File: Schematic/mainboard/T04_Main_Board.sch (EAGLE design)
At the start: 14 parts, among them IC1 7805DT, J1 AVR_SPI_PRG_6PTH, U1 ATMEGA328P_PDIP

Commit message: Mainboard Update and Prototype_rev4 update
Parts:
- removed C3, C4, C5: 0.1u, rcl:C-EUC3225
- removed X1, X2, X3: (no value), con-molex:KK-156-4
- added SV3: (no value), con-lsta:FE08-1
- added TP1, TP10, TP11, TP12, TP2, TP3, TP4, TP5, TP6, TP7, TP8, TP9: TPB1,27, testpad:TPB1,27
- C6: device rcl:C-EUC3225 -> rcl:C-EU025-024X044
- R1: value 4.7k -> 10k; device rcl:R-US_0414/5V -> rcl:R-US_M2309
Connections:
- removed net MISO/TRIG3: J1.1, U1.PB4(MISO), X3-1.S
- removed net MOSI/ECHO2: J1.4, U1.PB3(MOSI/OC2), X2-2.S
- removed net SCK/ECHO3: J1.3, U1.PB5(SCK), X3-2.S
- new net ECHO2: SV3.4, TP9.TP, U1.PD7(AIN1)
- new net ECHO3: SV3.6, TP11.TP, U1.PB1(OC1A)
- new net MISO: J1.1, U1.PB4(MISO)
- new net MOSI: J1.4, U1.PB3(MOSI/OC2)
- new net SCK: J1.3, U1.PB5(SCK)
- new net TRIG3: SV3.5, TP10.TP, U1.PB0(ICP)
- net +12V: now also TP12.TP
- net +5V: now also SV3.7, TP1.TP, U1.VCC; no longer C3.1, C4.1, C5.1, X1-3.S, X2-3.S, X3-3.S
- net BIT0: now also TP2.TP, U1.PD0(RXD); no longer U1.PD5(T1)
- net BIT1: now also TP3.TP, U1.PD1(TXD); no longer U1.PD6(AIN0)
- net BIT2: now also TP4.TP, U1.PD2(INT0); no longer U1.PD7(AIN1)
- net BIT3: now also TP5.TP, U1.PD3(INT1); no longer U1.PB0(ICP)
- net ECHO1: now also SV3.2, TP7.TP, U1.PD5(T1); no longer U1.PB1(OC1A), X1-2.S
- net GND: now also SV3.8, U1.GND@1, U1.GND@2; no longer C3.2, C4.2, C5.2, X1-4.S, X2-4.S, X3-4.S
- net TRIG1: now also SV3.1, TP6.TP, U1.PD4(XCK/T0); no longer U1.PD2(INT0), X1-1.S
- net TRIG2: now also SV3.3, TP8.TP, U1.PD6(AIN0); no longer U1.PB2(SS/OC1B), X2-1.S
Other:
- note added: "Connector To display.sch"
- note added: "Connector to programmer"
- note added: "Connnector to sensors"
- note added: "Rusty Wiseman Dan Frister Branden Driver Noah Erickson"
- note removed: "HEADER TO DISPLAY"
- note removed: "SENSOR 1"
- note removed: "SENSOR 2"
- note removed: "SENSOR 3"
- moved on the sheet: C1, C2, C6, IC1, J1, R1, SV1, U1

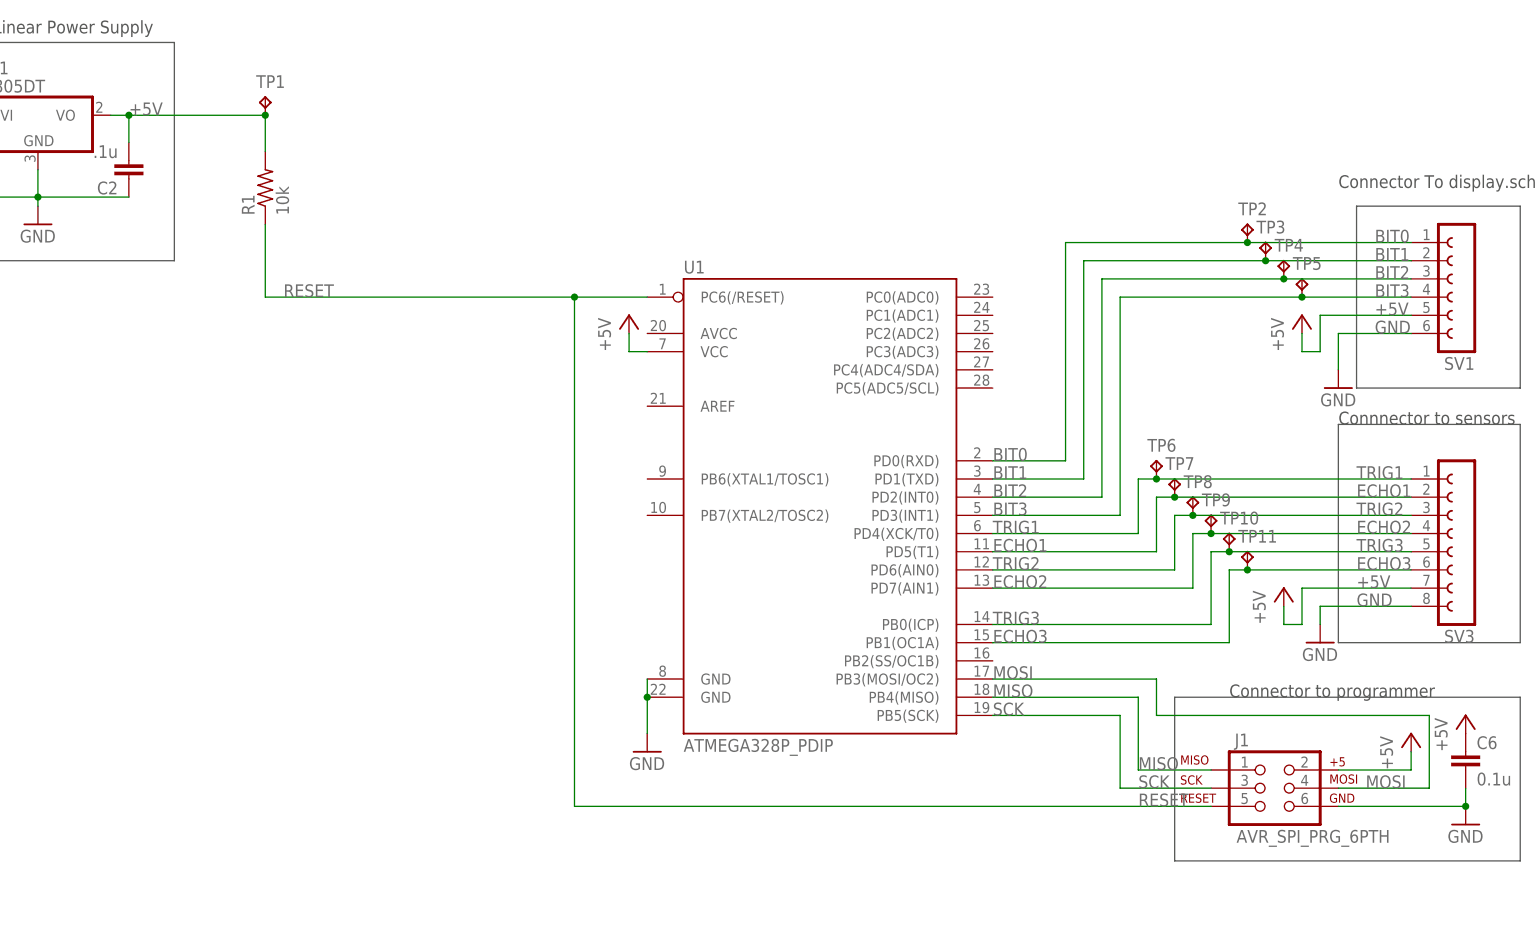
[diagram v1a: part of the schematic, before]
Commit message: Mainboard update - Clock and bypass caps
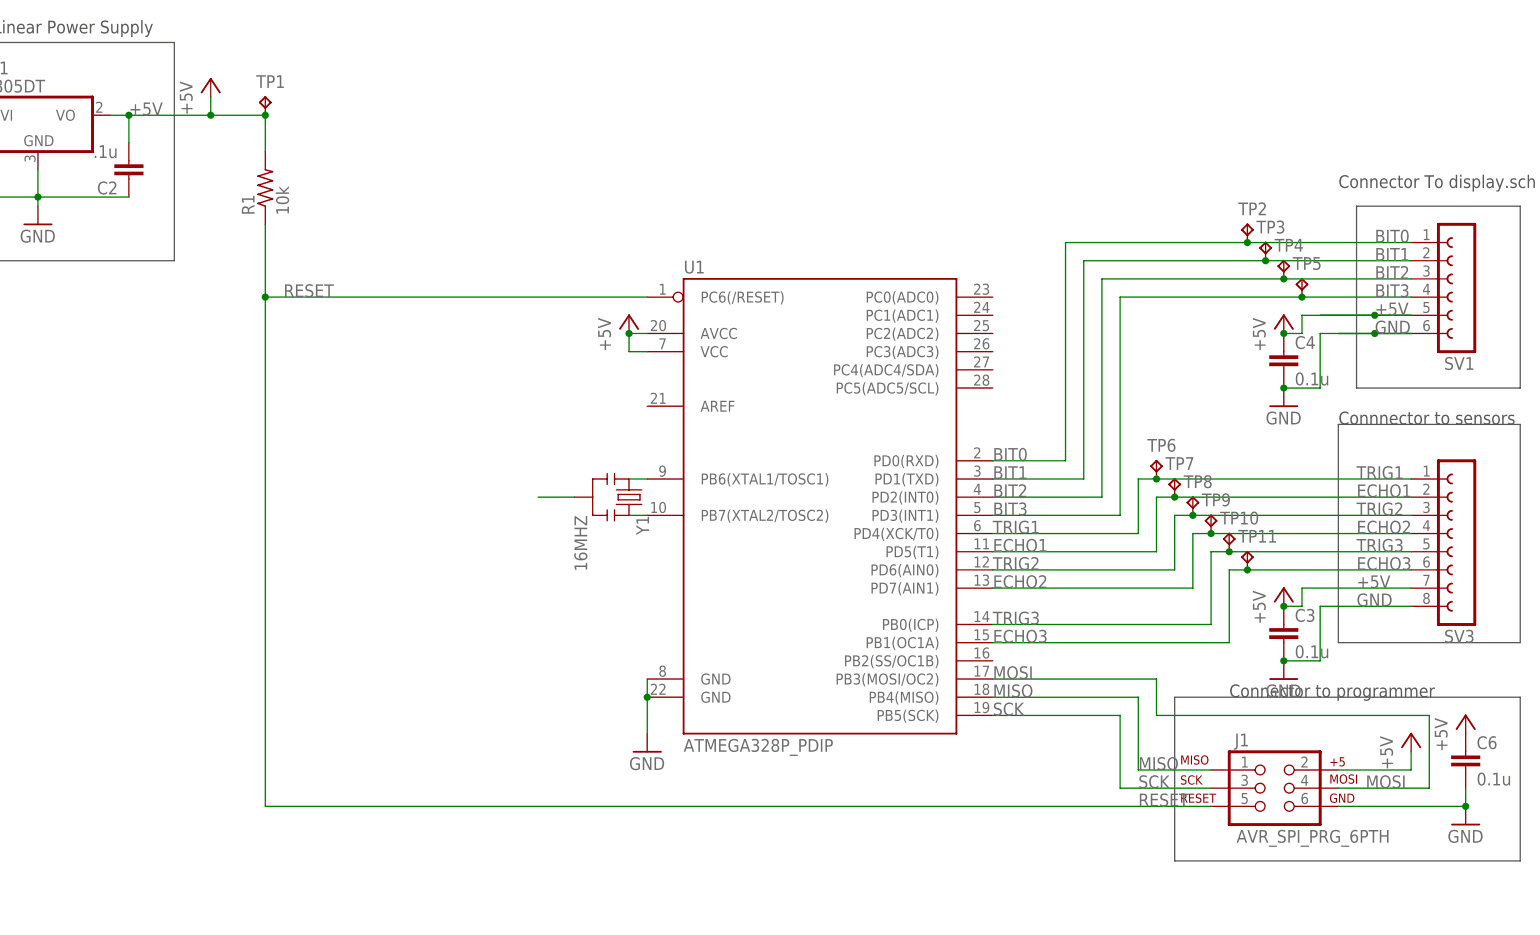
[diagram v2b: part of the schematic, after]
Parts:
- added C3, C4: 0.1u, rcl:C-EU025-024X044
- added Y1: 16MHZ, SparkFun-FreqCtrl:RESONATOR16MHZ
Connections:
- new net N$1: U1.PB6(XTAL1/TOSC1), Y1.1
- new net N$2: U1.PB7(XTAL2/TOSC2), Y1.3
- new net N$3: Y1.2
- net +5V: now also C3.1, C4.1, U1.AVCC
- net GND: now also C3.2, C4.2

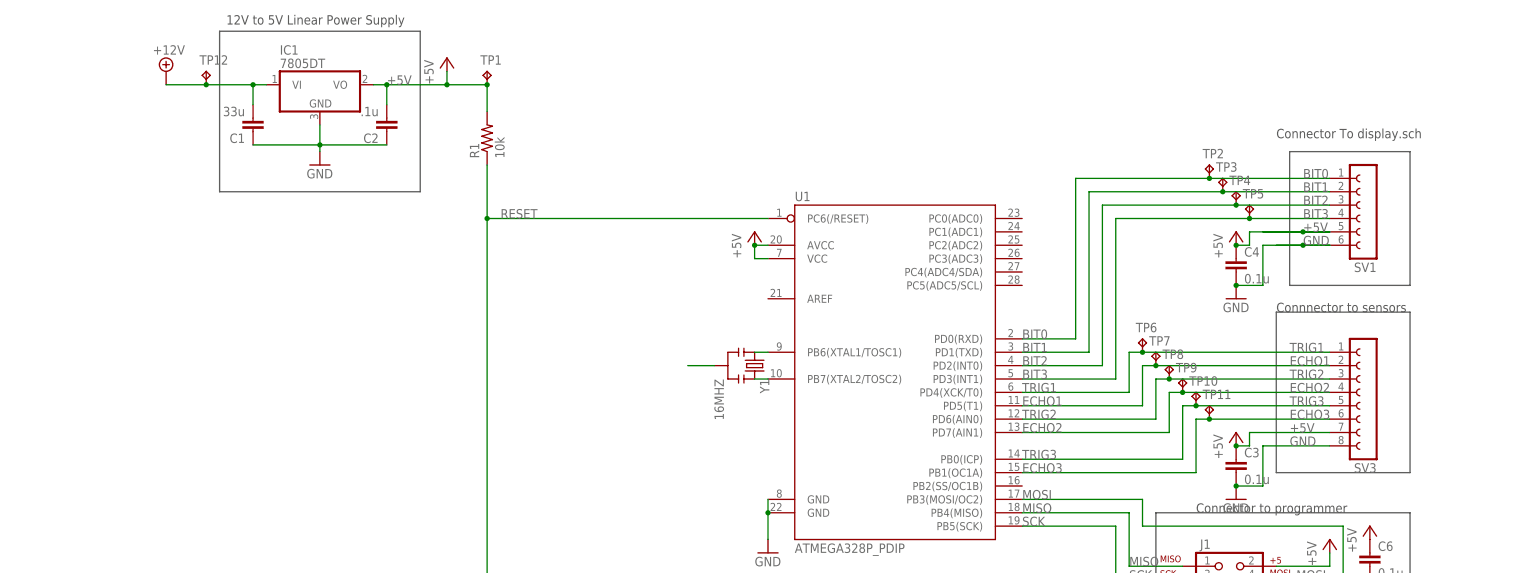
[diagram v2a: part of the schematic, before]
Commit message: Mainboard layout fixed
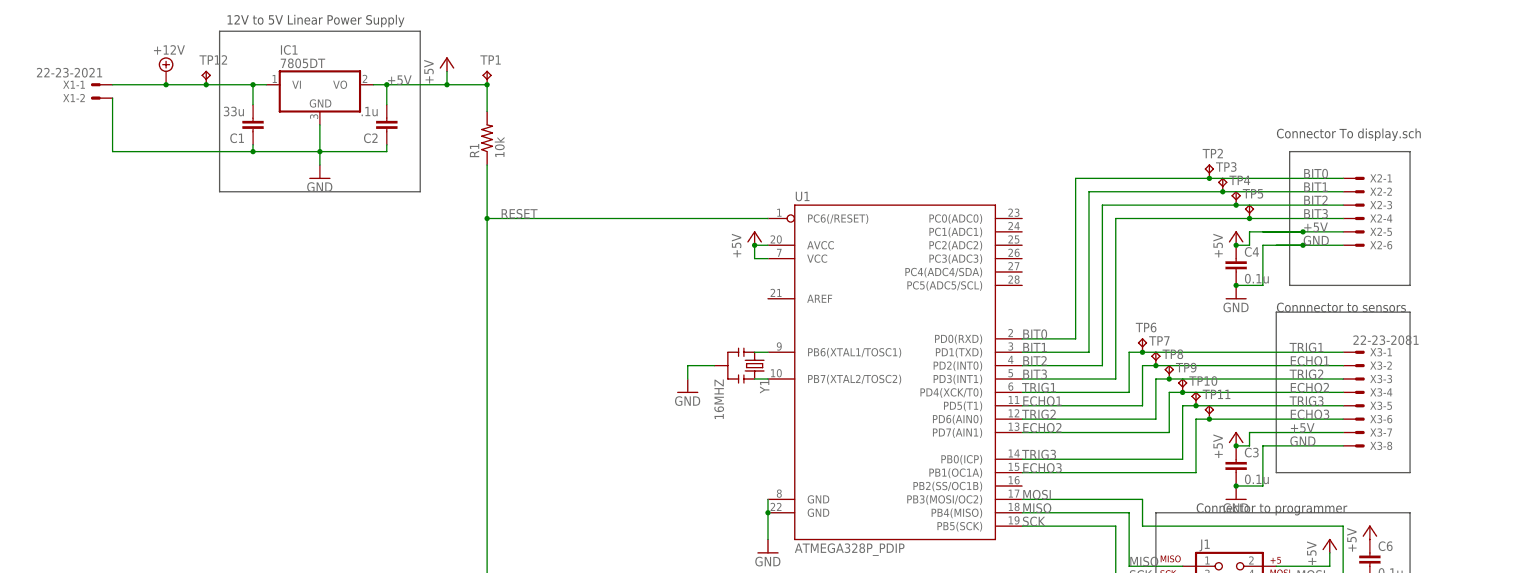
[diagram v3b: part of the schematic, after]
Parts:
- removed SV1: (no value), con-lsta:FE06-1
- removed SV3: (no value), con-lsta:FE08-1
- added X1: 22-23-2021, con-molex:22-23-2021
- added X2: (no value), con-molex:22-23-2061
- added X3: 22-23-2081, con-molex:22-23-2081
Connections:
- removed net N$3: Y1.2
- net +12V: now also X1-1.S
- net +5V: now also X2-5.S, X3-7.S; no longer SV1.5, SV3.7
- net BIT0: now also X2-1.S; no longer SV1.1
- net BIT1: now also X2-2.S; no longer SV1.2
- net BIT2: now also X2-3.S; no longer SV1.3
- net BIT3: now also X2-4.S; no longer SV1.4
- net ECHO1: now also X3-2.S; no longer SV3.2
- net ECHO2: now also X3-4.S; no longer SV3.4
- net ECHO3: now also X3-6.S; no longer SV3.6
- net GND: now also X1-2.S, X2-6.S, X3-8.S, Y1.2; no longer SV1.6, SV3.8
- net TRIG1: now also X3-1.S; no longer SV3.1
- net TRIG2: now also X3-3.S; no longer SV3.3
- net TRIG3: now also X3-5.S; no longer SV3.5

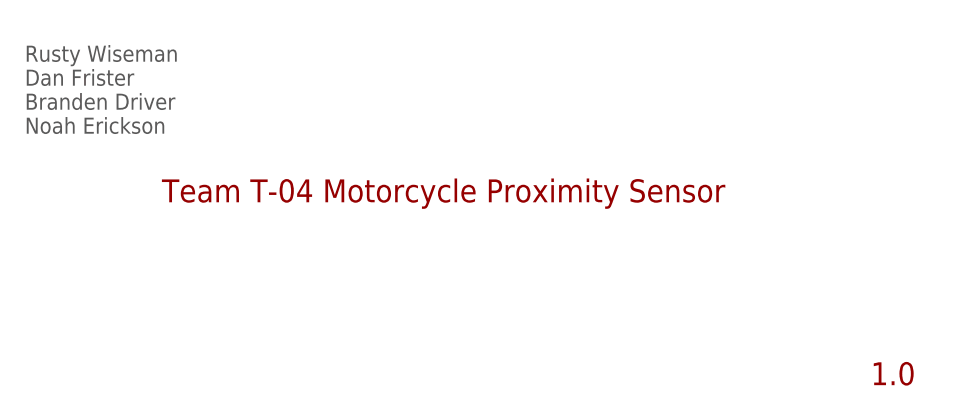
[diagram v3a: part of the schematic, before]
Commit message: Reverified ERC/DRC for assignment files, added version summery.
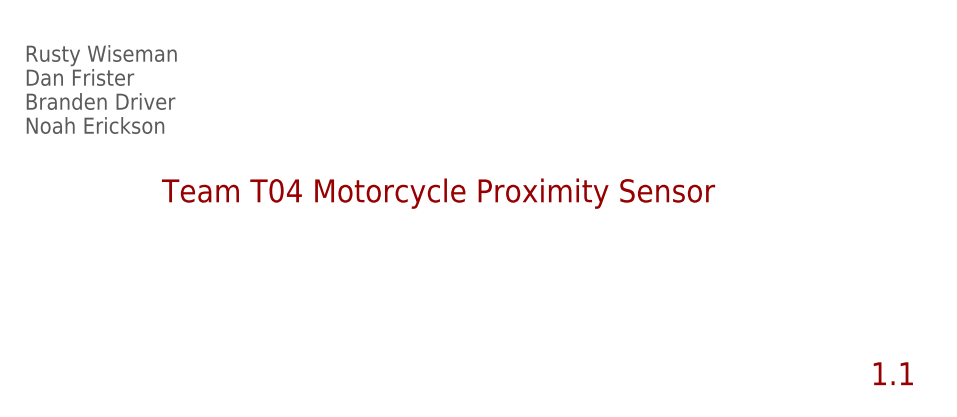
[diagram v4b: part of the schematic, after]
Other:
- note added: "1.1"
- note added: "Team T04 Motorcycle Proximity Sensor"
- note removed: "1.0"
- note removed: "Team T-04 Motorcycle Proximity Sensor"
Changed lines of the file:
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@@
 <?xml version="1.0" encoding="utf-8"?>
 <!DOCTYPE eagle SYSTEM "eagle.dtd">
-<eagle version="7.1.0">
+<eagle version="6.3">
 <drawing>
 <settings>
@@
 <setting verticaltext="up"/>
 </settings>
-<grid distance="0.05" unitdist="inch" unit="inch" style="lines" multiple="2" display="yes" altdistance="0.01" altunitdist="inch" altunit="inch"/>
+<grid distance="0.1" unitdist="inch" unit="inch" style="lines" multiple="1" display="no" altdistance="0.01" altunitdist="inch" altunit="inch"/>
 <layers>
-<layer number="1" name="Top" color="4" fill="1" visible="yes" active="no"/>
-<layer number="16" name="Bottom" color="1" fill="1" visible="yes" active="no"/>
-<layer number="17" name="Pads" color="2" fill="1" visible="yes" active="no"/>
-<layer number="18" name="Vias" color="2" fill="1" visible="yes" active="no"/>
-<layer number="19" name="Unrouted" color="6" fill="1" visible="yes" active="no"/>
-<layer number="20" name="Dimension" color="15" fill="1" visible="yes" active="no"/>
-<layer number="21" name="tPlace" color="7" fill="1" visible="yes" active="no"/>
-<layer number="22" name="bPlace" color="7" fill="1" visible="yes" active="no"/>
-<layer number="23" name="tOrigins" color="15" fill="1" visible="yes" active="no"/>
-<layer number="24" name="bOrigins" color="15" fill="1" visible="yes" active="no"/>
-<layer number="25" name="tNames" color="7" fill="1" visible="yes" active="no"/>
-<layer number="26" name="bNames" color="7" fill="1" visible="yes" active="no"/>
-<layer number="27" name="tValues" color="7" fill="1" visible="yes" active="no"/>
-<layer number="28" name="bValues" color="7" fill="1" visible="yes" active="no"/>
+<layer number="1" name="Top" color="4" fill="1" visible="no" active="no"/>
+<layer number="16" name="Bottom" color="1" fill="1" visible="no" active="no"/>
+<layer number="17" name="Pads" color="2" fill="1" visible="no" active="no"/>
+<layer number="18" name="Vias" color="2" fill="1" visible="no" active="no"/>
+<layer number="19" name="Unrouted" color="6" fill="1" visible="no" active="no"/>
+<layer number="20" name="Dimension" color="15" fill="1" visible="no" active="no"/>
+<layer number="21" name="tPlace" color="7" fill="1" visible="no" active="no"/>
+<layer number="22" name="bPlace" color="7" fill="1" visible="no" active="no"/>
+<layer number="23" name="tOrigins" color="15" fill="1" visible="no" active="no"/>
+<layer number="24" name="bOrigins" color="15" fill="1" visible="no" active="no"/>
+<layer number="25" name="tNames" color="7" fill="1" visible="no" active="no"/>
+<layer number="26" name="bNames" color="7" fill="1" visible="no" active="no"/>
+<layer number="27" name="tValues" color="7" fill="1" visible="no" active="no"/>
+<layer number="28" name="bValues" color="7" fill="1" visible="no" active="no"/>
 <layer number="29" name="tStop" color="7" fill="3" visible="no" active="no"/>
 <layer number="30" name="bStop" color="7" fill="6" visible="no" active="no"/>
@@
 <layer number="35" name="tGlue" color="7" fill="4" visible="no" active="no"/>
 <layer number="36" name="bGlue" color="7" fill="5" visible="no" active="no"/>
-<layer number="37" name="tTest" color="7" fill="1" visible="yes" active="no"/>
-<layer number="38" name="bTest" color="7" fill="1" visible="yes" active="no"/>
+<layer number="37" name="tTest" color="7" fill="1" visible="no" active="no"/>
+<layer number="38" name="bTest" color="7" fill="1" visible="no" active="no"/>
 <layer number="39" name="tKeepout" color="4" fill="11" visible="no" active="no"/>
 <layer number="40" name="bKeepout" color="1" fill="11" visible="no" active="no"/>
@@
 <layer number="44" name="Drills" color="7" fill="1" visible="no" active="no"/>
 <layer number="45" name="Holes" color="7" fill="1" visible="no" active="no"/>
-<layer number="46" name="Milling" color="3" fill="1" visible="yes" active="no"/>
-<layer number="47" name="Measures" color="7" fill="1" visible="yes" active="no"/>
-<layer number="48" name="Document" color="7" fill="1" visible="yes" active="no"/>
-<layer number="49" name="Reference" color="7" fill="1" visible="yes" active="no"/>
-<layer number="50" name="dxf" color="7" fill="1" visible="yes" active="no"/>
-<layer number="51" name="tDocu" color="7" fill="1" visible="yes" active="no"/>
-<layer number="52" name="bDocu" color="7" fill="1" visible="yes" active="no"/>
-<layer number="53" name="tGND_GNDA" color="7" fill="9" visible="yes" active="no"/>
-<layer number="54" name="bGND_GNDA" color="1" fill="9" visible="yes" active="no"/>
-<layer number="56" name="wert" color="7" fill="1" visible="yes" active="no"/>
-<layer number="57" name="tCAD" color="7" fill="1" visible="yes" active="no"/>
+<layer number="46" name="Milling" color="3" fill="1" visible="no" active="no"/>
+<layer number="47" name="Measures" color="7" fill="1" visible="no" active="no"/>
+<layer number="48" name="Document" color="7" fill="1" visible="no" active="no"/>
+<layer number="49" name="Reference" color="7" fill="1" visible="no" active="no"/>
+<layer number="50" name="dxf" color="7" fill="1" visible="no" active="no"/>
+<layer number="51" name="tDocu" color="7" fill="1" visible="no" active="no"/>
+<layer number="52" name="bDocu" color="7" fill="1" visible="no" active="no"/>
+<layer number="53" name="tGND_GNDA" color="7" fill="9" visible="no" active="no"/>
+<layer number="54" name="bGND_GNDA" color="1" fill="9" visible="no" active="no"/>
+<layer number="56" name="wert" color="7" fill="1" visible="no" active="no"/>
+<layer number="57" name="tCAD" color="7" fill="1" visible="no" active="no"/>
 <layer number="90" name="Modules" color="5" fill="1" visible="yes" active="yes"/>
 <layer number="91" name="Nets" color="2" fill="1" visible="yes" active="yes"/>
@@
 <wire x1="314.96" y1="177.8" x2="292.1" y2="177.8" width="0.1524" layer="97"/>
 <text x="289.56" y="180.34" size="1.778" layer="97">Connector To display.sch</text>
-<text x="340.36" y="27.94" size="2.54" layer="94">Team T-04 Motorcycle Proximity Sensor</text>
-<text x="419.1" y="7.62" size="2.54" layer="94">1.0</text>
+<text x="340.36" y="27.94" size="2.54" layer="94">Team T04 Motorcycle Proximity Sensor</text>
+<text x="419.1" y="7.62" size="2.54" layer="94">1.1</text>
 <text x="325.12" y="35.56" size="1.778" layer="97">Rusty Wiseman
 Dan Frister
